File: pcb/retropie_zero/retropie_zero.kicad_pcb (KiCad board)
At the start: 2 copper layers, 30 parts, among them J1 Conn_01x02_Socket, J2 Conn_01x10_Pin, SW1 SW_DIP_x01, SW10 SW_DIP_x01, SW11 SW_DIP_x01, SW12 SW_DIP_x01, SW13 SW_DIP_x01, SW14 SW_DIP_x01, SW2 SW_DIP_x01, SW3 SW_DIP_x01, SW4 SW_DIP_x01, SW5 SW_DIP_x01, SW6 SW_DIP_x01, SW7 SW_DIP_x01, SW8 SW_DIP_x01, SW9 SW_DIP_x01, U3 PAM8302AASCR, X1 TERMBLOCK_1X2

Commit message: PCB Routing finished
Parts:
- added SPC1: Button Spacer, lib:button_spacer, F.Cu at (221.5, 107.5)
- added SPC2: Button Spacer, lib:button_spacer, F.Cu at (115.0, 107.5)
- added U1: ~, Adafruit_2.2_SPI_240x320:TM022HDH26_2.2IN_LCD, B.Cu at (168.2, 104.5)
- added X2: TERMBLOCK_1X2, TerminalBlock_4Ucon:TerminalBlock_4Ucon_1x02_P3.50mm_Horizontal, F.Cu at (208.5, 126.1)
- SW10, SW11, SW12, SW9: footprint Button_Switch_THT:SW_PUSH_6mm -> Connector_PinHeader_2.54mm:PinHeader_1x02_P2.54mm_Vertical
- moved SW8 173.6 mm to (228.2, 105.2)
- moved SW7 171.4 mm to (218.2, 115.2)
- moved SW6 166.7 mm to (218.2, 95.2)
- moved SW5 159.7 mm to (208.2, 105.2)
- moved SW11 150.1 mm to (210.7, 95.2), turned to 90 degrees
- moved J2 145.7 mm to (203.8, 97.4)
- moved SW12 144.7 mm to (210.8, 89.2), turned to 90 degrees
- moved U1 126.6 mm to (163.7, 113.4), turned to -90 degrees
- moved SW14 126.3 mm to (177.2, 131.2)
- moved SW13 116.2 mm to (156.8, 131.2)
- moved X1 102.3 mm to (145.6, 133.8)
- moved J1 89.8 mm to (134.4, 132.3), turned to 90 degrees
- moved SW3 88.4 mm to (121.8, 105.2)
- moved SW1 86.0 mm to (111.8, 95.2)
- moved SW4 81.9 mm to (111.8, 115.2)
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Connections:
- net PowerBoost Ground renamed GND
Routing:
- net R_TRIG: track 0.00 -> 105.0 mm, vias 0 -> 3
- net SW_X: track 0.00 -> 92.2 mm
- net SW_B: track 0.00 -> 73.0 mm, vias 0 -> 1
- net AIN +: track 0.00 -> 72.9 mm
- net PowerBoost Power: track 0.00 -> 71.2 mm, vias 0 -> 1
- net +3V3: track 0.00 -> 70.9 mm
- net R_BUMP: track 0.00 -> 64.4 mm
- net DPAD_L: track 0.00 -> 63.4 mm
- net SW_A: track 0.00 -> 61.5 mm
- net SW_Y: track 0.00 -> 53.4 mm
- net SCREEN_RST: track 0.00 -> 52.7 mm
- net SCREEN_D_C: track 0.00 -> 49.1 mm
- net L_BUMP: track 0.00 -> 49.0 mm
- net SCREEN_CLK: track 0.00 -> 47.5 mm
- net SCREEN_MOSI: track 0.00 -> 45.4 mm
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- added copper zone on B.Cu, net GND
- added copper zone on F.Cu, net GND
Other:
- board outline added: 166.8 x 82.8 mm

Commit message: Wiring finished
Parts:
- removed SPC1, SPC2: Button Spacer, lib:button_spacer
- moved R3 0.60 mm to (132.1, 122.6)
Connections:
- SW10 pad 2: R_TRIG -> L_TRIG
- U1 pad 10: R_TRIG -> L_TRIG
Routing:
- net AIN -: track 10.0 -> 91.5 mm
- net L_TRIG: track 0.00 -> 42.7 mm
- net R_TRIG: track 105.0 -> 62.2 mm
- net GND: track 0.00 -> 25.6 mm, vias 0 -> 5
- net PowerBoost Power: track 71.2 -> 72.5 mm
- net SW_STA: track 32.8 -> 33.9 mm
- net VCC: track 19.6 -> 19.0 mm
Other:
- board size 166.8 x 82.8 mm -> 136.8 x 54.2 mm

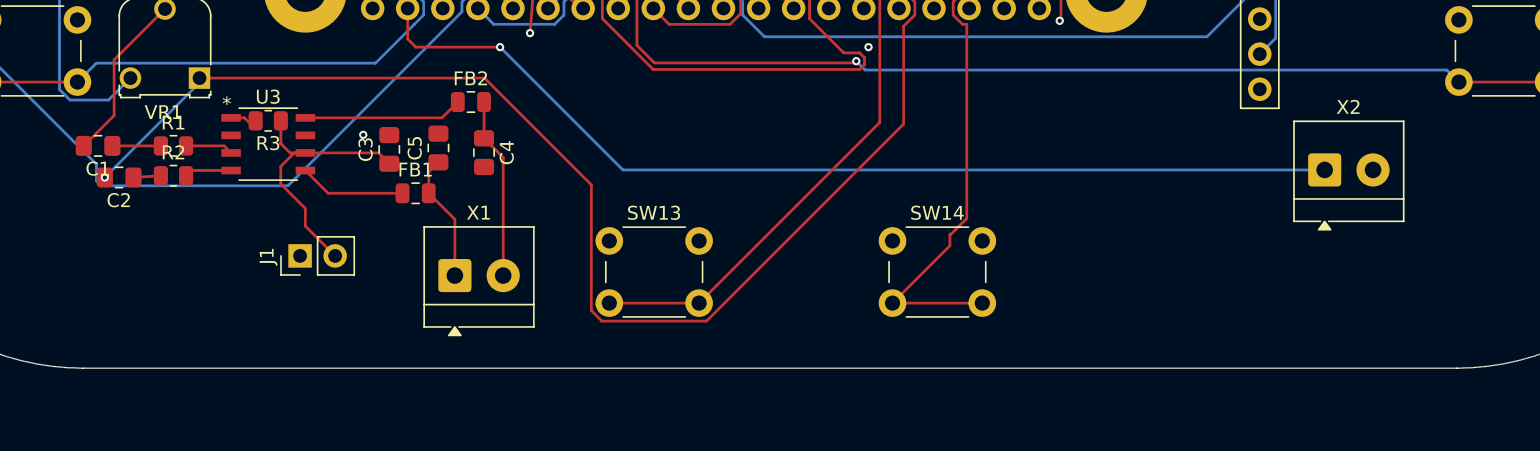
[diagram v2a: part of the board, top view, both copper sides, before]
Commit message: Board Outline Fixed
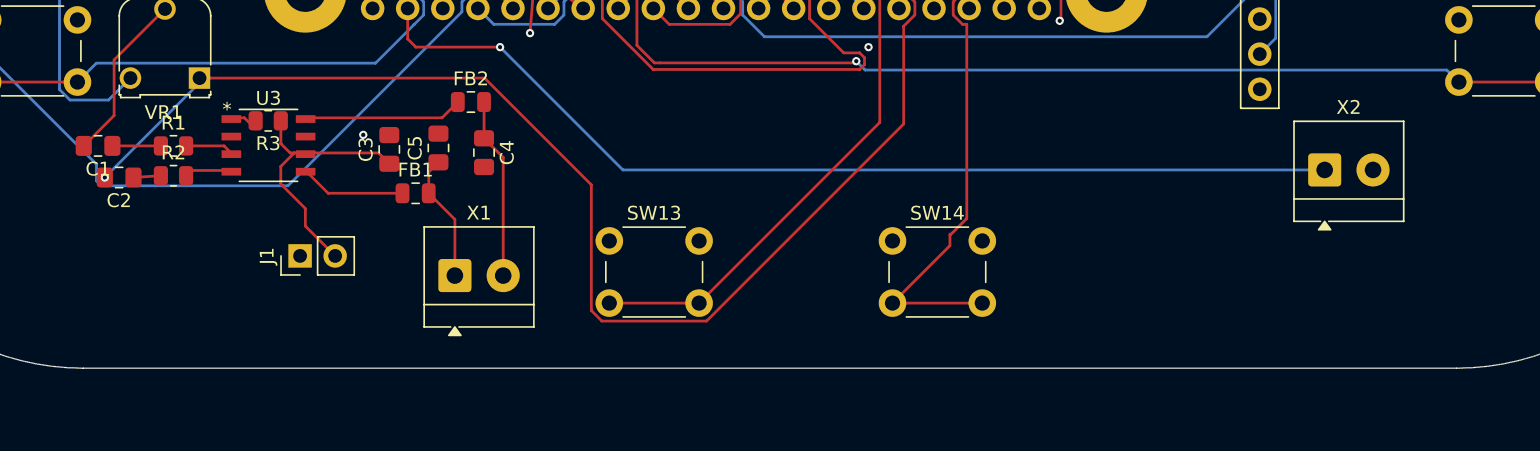
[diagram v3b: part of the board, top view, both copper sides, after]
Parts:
- moved U3 0.09 mm to (132.1, 124.3)

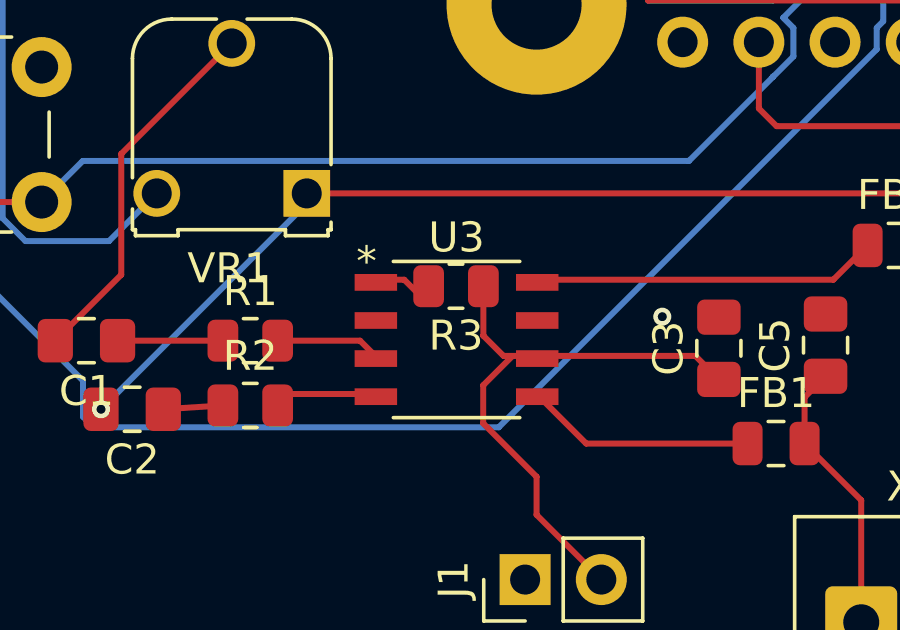
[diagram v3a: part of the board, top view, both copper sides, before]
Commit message: Fixed resistor placement
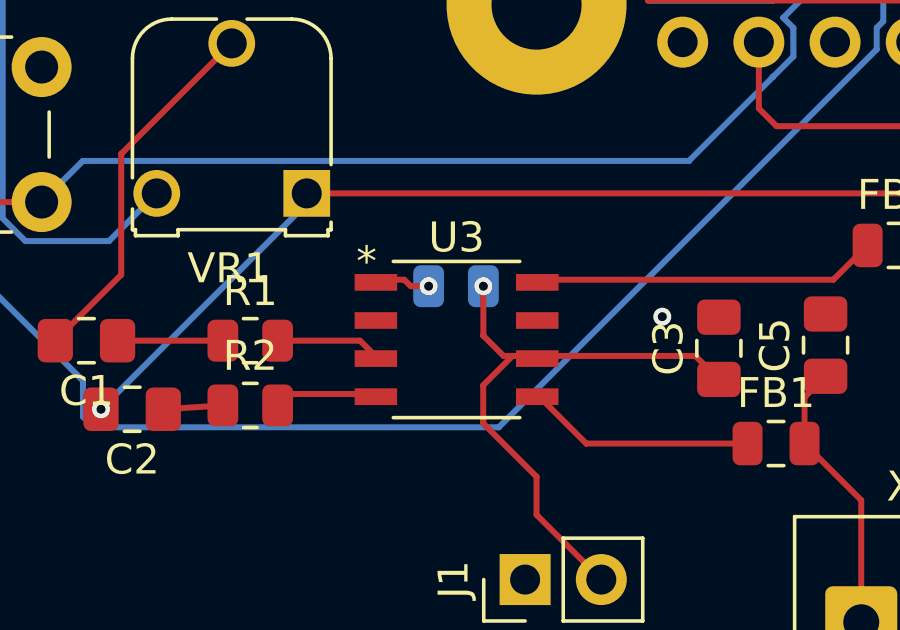
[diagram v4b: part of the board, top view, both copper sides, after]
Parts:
- R3: moved to B.Cu
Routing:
- net VCC: track 19.0 -> 19.6 mm, vias 0 -> 1
- net /SD: track 2.11 -> 1.87 mm, vias 0 -> 1
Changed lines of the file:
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@@
 		)
 	)
-	(footprint "Resistor_SMD:R_0805_2012Metric"
-		(layer "F.Cu")
-		(at 132.062 122.555 180)
-		(descr "Resistor SMD 0805 (2012 Metric), square (rectangular) end terminal, IPC-7351 nominal, (Body size source: IPC-SM-782 page 72, https://www.pcb-3d.com/wordpress/wp-content/uploads/ipc-sm-782a_amendment_1_and_2.pdf), generated with kicad-footprint-generator")
-		(tags "resistor")
-		(property "Reference" "R3"
-			(at 0 -1.65 0)
-			(layer "F.SilkS")
-			(effects
-				(font
-					(size 1 1)
-					(thickness 0.15)
-				)
-			)
-		)
-		(property "Value" "10K"
-			(at 0 1.65 0)
-			(layer "F.Fab")
-			(effects
-				(font
-					(size 1 1)
-					(thickness 0.15)
-				)
-			)
-		)
-		(property "Datasheet" ""
-			(at 0 0 0)
-			(layer "F.Fab")
-			(hide yes)
-			(effects
-				(font
-					(size 1.27 1.27)
-					(thickness 0.15)
-				)
-			)
-		)
-		(property "Description" ""
-			(at 0 0 0)
-			(layer "F.Fab")
-			(hide yes)
-			(effects
-				(font
-					(size 1.27 1.27)
-					(thickness 0.15)
-				)
-			)
-		)
-		(sheetname "/")
-		(sheetfile "retropie_zero.kicad_sch")
-		(attr smd)
-		(fp_line
-			(start -0.227064 0.735)
-			(end 0.227064 0.735)
-			(stroke
-				(width 0.12)
-				(type solid)
-			)
-			(layer "F.SilkS")
-		)
-		(fp_line
-			(start -0.227064 -0.735)
-			(end 0.227064 -0.735)
-			(stroke
-				(width 0.12)
-				(type solid)
-			)
-			(layer "F.SilkS")
-		)
-		(fp_line
-			(start 1.68 0.95)
-			(end -1.68 0.95)
-			(stroke
-				(width 0.05)
-				(type solid)
-			)
-			(layer "F.CrtYd")
-		)
-		(fp_line
-			(start 1.68 -0.95)
-			(end 1.68 0.95)
-			(stroke
-				(width 0.05)
-				(type solid)
-			)
-			(layer "F.CrtYd")
-		)
-		(fp_line
-			(start -1.68 0.95)
-			(end -1.68 -0.95)
-			(stroke
-				(width 0.05)
-				(type solid)
-			)
-			(layer "F.CrtYd")
-		)
-		(fp_line
-			(start -1.68 -0.95)
-			(end 1.68 -0.95)
-			(stroke
-				(width 0.05)
-				(type solid)
-			)
-			(layer "F.CrtYd")
-		)
-		(fp_line
-			(start 1 0.625)
-			(end -1 0.625)
-			(stroke
-				(width 0.1)
-				(type solid)
-			)
-			(layer "F.Fab")
-		)
-		(fp_line
-			(start 1 -0.625)
-			(end 1 0.625)
-			(stroke
-				(width 0.1)
-				(type solid)
-			)
-			(layer "F.Fab")
-		)
-		(fp_line
-			(start -1 0.625)
-			(end -1 -0.625)
-			(stroke
-				(width 0.1)
-				(type solid)
-			)
-			(layer "F.Fab")
-		)
-		(fp_line
-			(start -1 -0.625)
-			(end 1 -0.625)
-			(stroke
-				(width 0.1)
-				(type solid)
-			)
-			(layer "F.Fab")
-		)
-		(fp_text user "${REFERENCE}"
-			(at 0 0 0)
-			(layer "F.Fab")
-			(effects
-				(font
-					(size 0.5 0.5)
-					(thickness 0.08)
-				)
-			)
-		)
-		(pad "1" smd roundrect
-			(at -0.9125 0 180)
-			(size 1.025 1.4)
-			(layers "F.Cu" "F.Mask" "F.Paste")
-			(roundrect_rratio 0.243902)
-			(net 1 "VCC")
-			(pinfunction "1")
-			(pintype "passive")
-		)
-		(pad "2" smd roundrect
-			(at 0.9125 0 180)
-			(size 1.025 1.4)
-			(layers "F.Cu" "F.Mask" "F.Paste")
-			(roundrect_rratio 0.243902)
-			(net 44 "/SD")
-			(pinfunction "2")
-			(pintype "passive")
-		)
-		(embedded_fonts no)
-		(model "${KICAD9_3DMODEL_DIR}/Resistor_SMD.3dshapes/R_0805_2012Metric.wrl"
-			(offset
-				(xyz 0 0 0)
-			)
-			(scale
-				(xyz 1 1 1)
-			)
-			(rotate
-				(xyz 0 0 0)
-			)
-		)
-	)
 	(footprint "Capacitor_SMD:C_0805_2012Metric_Pad1.18x1.45mm_HandSolder"
 		(layer "F.Cu")
@@
 		)
 	)
+	(footprint "Resistor_SMD:R_0805_2012Metric"
+		(layer "B.Cu")
+		(at 132.062 122.555 180)
+		(descr "Resistor SMD 0805 (2012 Metric), square (rectangular) end terminal, IPC-7351 nominal, (Body size source: IPC-SM-782 page 72, https://www.pcb-3d.com/wordpress/wp-content/uploads/ipc-sm-782a_amendment_1_and_2.pdf), generated with kicad-footprint-generator")
+		(tags "resistor")
+		(property "Reference" "R3"
+			(at 0 1.65 0)
+			(layer "B.SilkS")
+			(effects
+				(font
+					(size 1 1)
+					(thickness 0.15)
+				)
+				(justify mirror)
+			)
+		)
+		(property "Value" "10K"
+			(at 0 -1.65 0)
+			(layer "B.Fab")
+			(effects
+				(font
+					(size 1 1)
+					(thickness 0.15)
+				)
+				(justify mirror)
+			)
+		)
+		(property "Datasheet" ""
+			(at 0 0 0)
+			(layer "B.Fab")
+			(hide yes)
+			(effects
+				(font
+					(size 1.27 1.27)
+					(thickness 0.15)
+				)
+				(justify mirror)
+			)
+		)
+		(property "Description" ""
+			(at 0 0 0)
+			(layer "B.Fab")
+			(hide yes)
+			(effects
+				(font
+					(size 1.27 1.27)
+					(thickness 0.15)
+				)
+				(justify mirror)
+			)
+		)
+		(sheetname "/")
+		(sheetfile "retropie_zero.kicad_sch")
+		(attr smd)
+		(fp_line
+			(start -0.227064 0.735)
+			(end 0.227064 0.735)
+			(stroke
+				(width 0.12)
+				(type solid)
+			)
+			(layer "B.SilkS")
+		)
+		(fp_line
+			(start -0.227064 -0.735)
+			(end 0.227064 -0.735)
+			(stroke
+				(width 0.12)
+				(type solid)
+			)
+			(layer "B.SilkS")
+		)
+		(fp_line
+			(start 1.68 0.95)
+			(end 1.68 -0.95)
+			(stroke
+				(width 0.05)
+				(type solid)
+			)
+			(layer "B.CrtYd")
+		)
+		(fp_line
+			(start 1.68 -0.95)
+			(end -1.68 -0.95)
+			(stroke
+				(width 0.05)
+				(type solid)
+			)
+			(layer "B.CrtYd")
+		)
+		(fp_line
+			(start -1.68 0.95)
+			(end 1.68 0.95)
+			(stroke
+				(width 0.05)
+				(type solid)
+			)
+			(layer "B.CrtYd")
+		)
+		(fp_line
+			(start -1.68 -0.95)
+			(end -1.68 0.95)
+			(stroke
+				(width 0.05)
+				(type solid)
+			)
+			(layer "B.CrtYd")
+		)
+		(fp_line
+			(start 1 0.625)
+			(end 1 -0.625)
+			(stroke
+				(width 0.1)
+				(type solid)
+			)
+			(layer "B.Fab")
+		)
+		(fp_line
+			(start 1 -0.625)
+			(end -1 -0.625)
+			(stroke
+				(width 0.1)
+				(type solid)
+			)
+			(layer "B.Fab")
+		)
+		(fp_line
+			(start -1 0.625)
+			(end 1 0.625)
+			(stroke
+				(width 0.1)
+				(type solid)
+			)
+			(layer "B.Fab")
+		)
+		(fp_line
+			(start -1 -0.625)
+			(end -1 0.625)
+			(stroke
+				(width 0.1)
+				(type solid)
+			)
+			(layer "B.Fab")
+		)
+		(fp_text user "${REFERENCE}"
+			(at 0 0 0)
+			(layer "B.Fab")
+			(effects
+				(font
+					(size 0.5 0.5)
+					(thickness 0.08)
+				)
+				(justify mirror)
+			)
+		)
+		(pad "1" smd roundrect
+			(at -0.9125 0 180)
+			(size 1.025 1.4)
+			(layers "B.Cu" "B.Mask" "B.Paste")
+			(roundrect_rratio 0.243902)
+			(net 1 "VCC")
+			(pinfunction "1")
+			(pintype "passive")
+		)
+		(pad "2" smd roundrect
+			(at 0.9125 0 180)
+			(size 1.025 1.4)
+			(layers "B.Cu" "B.Mask" "B.Paste")
+			(roundrect_rratio 0.243902)
+			(net 44 "/SD")
+			(pinfunction "2")
+			(pintype "passive")
+		)
+		(embedded_fonts no)
+		(model "${KICAD9_3DMODEL_DIR}/Resistor_SMD.3dshapes/R_0805_2012Metric.wrl"
+			(offset
+				(xyz 0 0 0)
+			)
+			(scale
+				(xyz 1 1 1)
+			)
+			(rotate
+				(xyz 0 0 0)
+			)
+		)
+	)
 	(gr_line
 		(start 100 96.25)
@@
 	)
 	(segment
+		(start 132.9745 122.555)
+		(end 132.9745 124.206)
+		(width 0.2)
+		(layer "F.Cu")
+		(net 1)
+	)
+	(segment
 		(start 133.947 124.879)
 		(end 133.6475 124.879)
@@
 	)
 	(segment
-		(start 132.9745 123.151701)
-		(end 132.9745 124.206)
-		(width 0.2)
-		(layer "F.Cu")
-		(net 1)
-	)
-	(segment
 		(start 134.747 130.175)
 		(end 136.906 132.334)
@@
 		(net 1)
 	)
+	(via
+		(at 132.9745 122.555)
+		(size 0.6)
+		(drill 0.3)
+		(layers "F.Cu" "B.Cu")
+		(net 1)
+	)
 	(segment
 		(start 189.446 115.227)
@@
 	)
 	(segment
-		(start 130.336799 122.339)
-		(end 131.1495 123.151701)
+		(start 130.552799 122.555)
+		(end 130.336799 122.339)
+		(width 0.2)
+		(layer "F.Cu")
+		(net 44)
+	)
+	(segment
+		(start 131.1495 122.555)
+		(end 130.552799 122.555)
 		(width 0.2)
 		(layer "F.Cu")
 		(net 44)
 	)
+	(via
+		(at 131.1495 122.555)
+		(size 0.6)
+		(drill 0.3)
+		(layers "F.Cu" "B.Cu")
+		(net 44)
+	)
